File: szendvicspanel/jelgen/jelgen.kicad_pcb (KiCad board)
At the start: 2 copper layers, 23 parts, among them J1 Conn_01x04_Pin, U1 TL072, U2 TL072

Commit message: PCB sketch 2
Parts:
- removed TJ1, TJ2, TJ3: Conn_01x01_Pin, Connector_PinHeader_2.54mm:PinHeader_1x01_P2.54mm_Vertical
- added TP1: TestPoint, Connector_PinHeader_2.54mm:PinHeader_1x01_P2.54mm_Vertical, F.Cu at (149.0, 73.0)
- added TP2: TestPoint, Connector_PinHeader_2.54mm:PinHeader_1x01_P2.54mm_Vertical, F.Cu at (112.0, 66.0)
- added TP3: TestPoint, Connector_PinHeader_2.54mm:PinHeader_1x01_P2.54mm_Vertical, F.Cu at (112.0, 58.5)
- added TP4: TestPoint, Connector_PinHeader_2.54mm:PinHeader_1x01_P2.54mm_Vertical, F.Cu at (112.0, 73.5)
- J1: footprint Connector_PinHeader_2.54mm:PinHeader_1x04_P2.54mm_Horizontal -> Connector_PinHeader_2.54mm:PinHeader_1x04_P2.54mm_Vertical
- moved RV2 67.2 mm to (136.1, 65.3)
- moved U1 67.2 mm to (122.6, 62.4)
- moved C1 67.2 mm to (141.6, 52.4)
- moved R1 67.2 mm to (134.1, 58.4)
- moved R2 67.2 mm to (136.6, 74.9)
- moved R3 67.2 mm to (144.6, 60.9)
- moved RV3 67.2 mm to (142.6, 70.4)
- moved J1 45.3 mm to (78.0, 65.0), turned to 0 degrees
- moved C2 43.0 mm to (94.0, 75.0)
- moved R4 43.0 mm to (97.0, 67.0)
- moved RV1 43.0 mm to (90.9, 61.5)
- moved U2 42.0 mm to (101.0, 62.0)
- moved OJ1 13.9 mm to (78.0, 49.5)
- moved OJ2 13.9 mm to (85.5, 49.5)
- moved OJ3 13.9 mm to (93.0, 49.5)
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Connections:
- OJ1 pad 1: /PWM -> GND
- OJ1 pad 3: GND -> /OUT_ARRAY_PIN3
- OJ2 pad 1: /PWM -> GND
- OJ2 pad 3: GND -> /OUT_ARRAY_PIN3
- OJ3 pad 1: /PWM -> GND
- OJ3 pad 3: GND -> /OUT_ARRAY_PIN3
- OJ4 pad 1: /PWM -> GND
- OJ4 pad 3: GND -> /OUT_ARRAY_PIN3
- OJ5 pad 1: /PWM -> GND
- OJ5 pad 3: GND -> /OUT_ARRAY_PIN3
- OJ6 pad 1: /PWM -> GND
- OJ6 pad 3: GND -> /OUT_ARRAY_PIN3
- OJ7 pad 1: /PWM -> GND
- OJ7 pad 3: GND -> /OUT_ARRAY_PIN3
- OJ8 pad 1: /PWM -> GND
- OJ8 pad 3: GND -> /OUT_ARRAY_PIN3
- U2 pad 7: /PWM -> /OUT_ARRAY_PIN3
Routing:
- net /PWM: track 81.4 -> 0.00 mm
- net VPWR: track 215.8 -> 142.2 mm
- net /OUT_ARRAY_PIN3: track 0.00 -> 65.4 mm
- net /REF: track 63.1 -> 50.8 mm
- net /ANALOG_IN: track 22.3 -> 18.0 mm
- net /SQUARE: track 5.22 -> 6.42 mm
- net /TRIANGLE: track 34.1 -> 35.1 mm
- net Net-(U2A-+): track 12.8 -> 11.8 mm
- net GND: track 177.7 -> 178.4 mm
- net Net-(U1B-+): track 36.7 -> 37.4 mm
- net Net-(U1A--): track 30.9 -> 30.4 mm
- net Net-(U2B-+): track 20.2 -> 19.7 mm
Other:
- board outline added: 85 x 40 mm

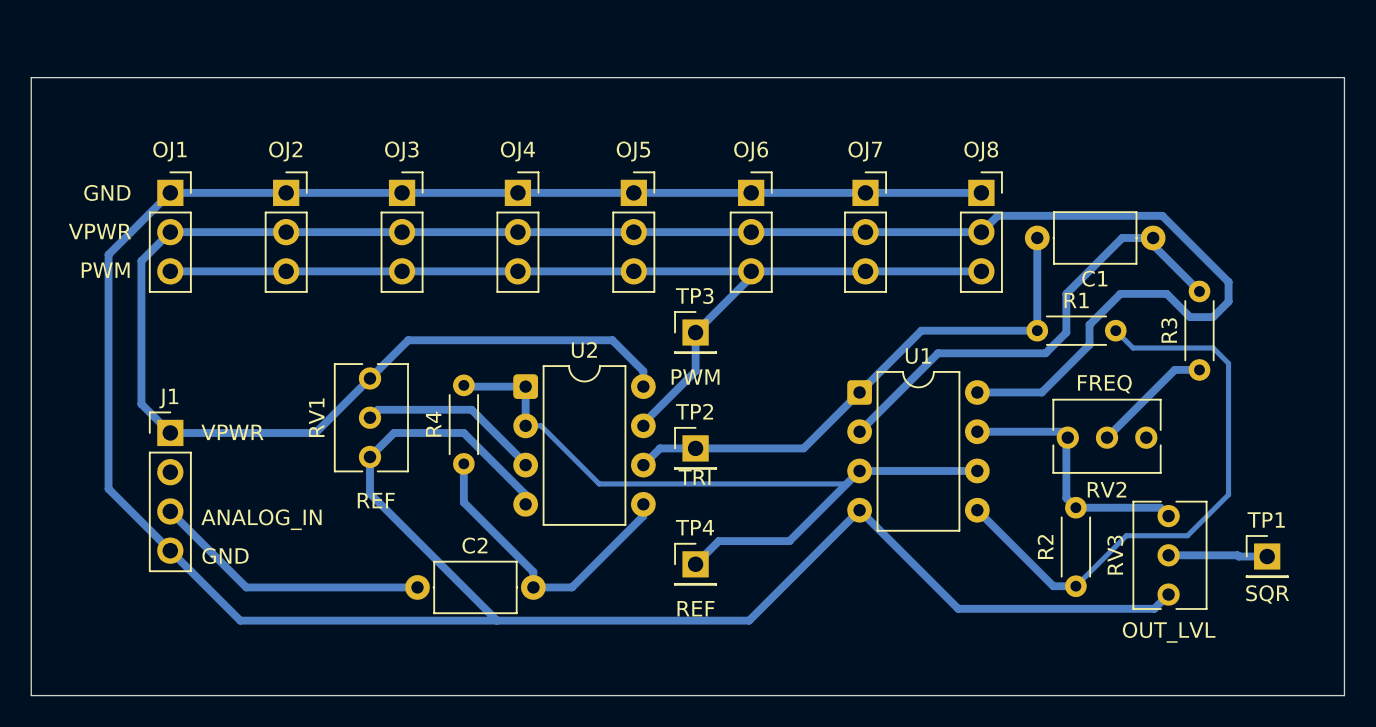
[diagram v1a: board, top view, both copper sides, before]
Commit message: Ground plane, output array áttervezés, input horizontal footprint
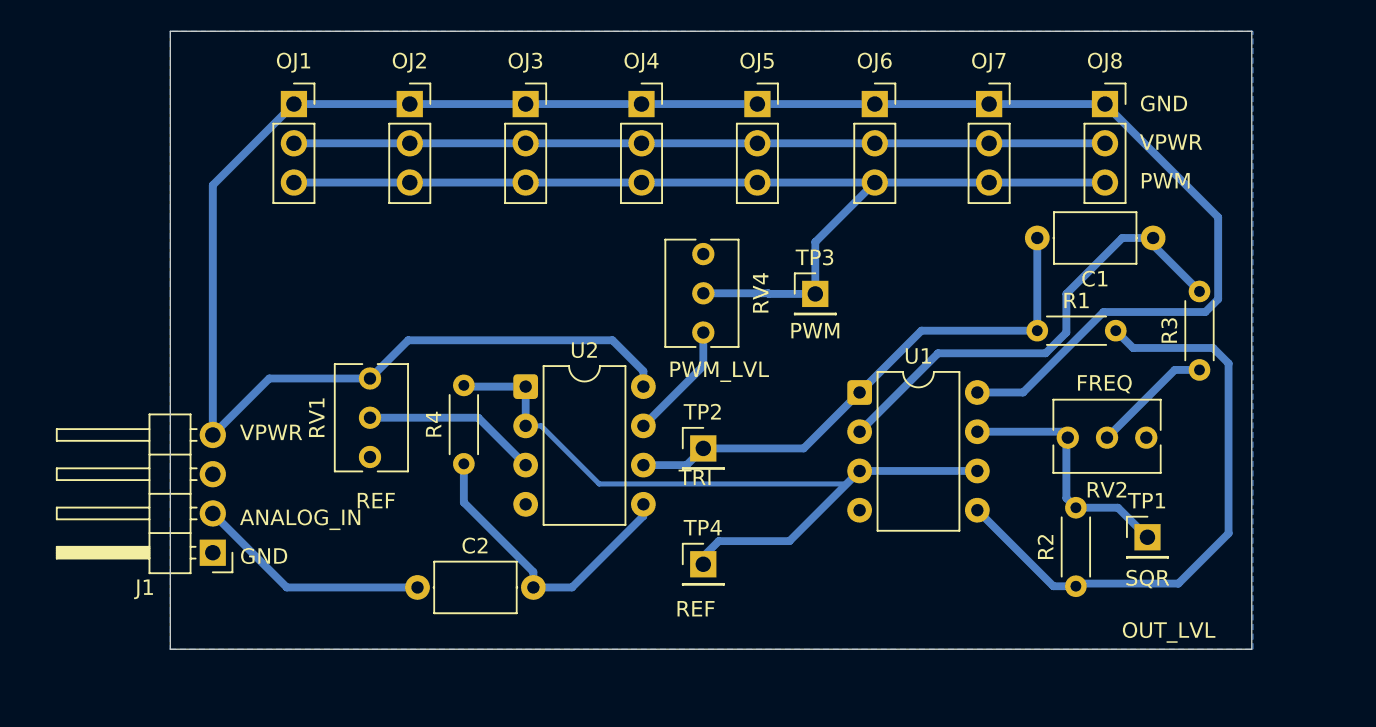
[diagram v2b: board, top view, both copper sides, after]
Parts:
- removed RV3: R_Potentiometer, Potentiometer_THT:Potentiometer_Bourns_3266Y_Vertical
- added RV4: R_Potentiometer, Potentiometer_THT:Potentiometer_Bourns_3266Y_Vertical, F.Cu at (112.5, 58.5)
- J1: footprint Connector_PinHeader_2.54mm:PinHeader_1x04_P2.54mm_Vertical -> Connector_PinHeader_2.54mm:PinHeader_1x04_P2.54mm_Horizontal
- moved OJ1 9.85 mm to (86.0, 43.7)
- moved OJ2 9.85 mm to (93.5, 43.7)
- moved OJ3 9.85 mm to (101.0, 43.7)
- moved OJ4 9.85 mm to (108.5, 43.7)
- moved OJ5 9.85 mm to (116.0, 43.7)
- moved OJ6 9.85 mm to (123.6, 43.7)
- moved OJ7 9.85 mm to (131.0, 43.7)
- moved OJ8 9.85 mm to (138.5, 43.7)
- moved J1 8.22 mm to (80.8, 72.8), turned to 180 degrees
- moved TP3 8.14 mm to (119.8, 56.0)
- moved TP1 7.85 mm to (141.2, 71.8)
- moved TP2 0.50 mm to (112.5, 66.0)
- moved TP4 0.50 mm to (112.5, 73.5)
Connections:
- J1 pad 1: VPWR -> GND
- J1 pad 2: unconnected-(J1-Pin_2-Pad2) -> /ANALOG_IN
- J1 pad 3: /ANALOG_IN -> unconnected-(J1-Pin_3-Pad3)
- J1 pad 4: GND -> VPWR
- OJ1 pad 1: GND -> VPWR
- OJ1 pad 2: VPWR -> GND
- OJ1 pad 3: /OUT_ARRAY_PIN3 -> /PWM
- OJ2 pad 1: GND -> VPWR
- OJ2 pad 2: VPWR -> GND
- OJ2 pad 3: /OUT_ARRAY_PIN3 -> /PWM
- OJ3 pad 1: GND -> VPWR
- OJ3 pad 2: VPWR -> GND
- OJ3 pad 3: /OUT_ARRAY_PIN3 -> /PWM
- OJ4 pad 1: GND -> VPWR
- OJ4 pad 2: VPWR -> GND
- OJ4 pad 3: /OUT_ARRAY_PIN3 -> /PWM
- OJ5 pad 1: GND -> VPWR
- OJ5 pad 2: VPWR -> GND
- OJ5 pad 3: /OUT_ARRAY_PIN3 -> /PWM
- OJ6 pad 1: GND -> VPWR
- OJ6 pad 2: VPWR -> GND
- OJ6 pad 3: /OUT_ARRAY_PIN3 -> /PWM
- OJ7 pad 1: GND -> VPWR
- OJ7 pad 2: VPWR -> GND
- OJ7 pad 3: /OUT_ARRAY_PIN3 -> /PWM
- OJ8 pad 1: GND -> VPWR
- OJ8 pad 2: VPWR -> GND
- OJ8 pad 3: /OUT_ARRAY_PIN3 -> /PWM
- R2 pad 2: Net-(R2-Pad2) -> /SQUARE
- RV2 pad 1: Net-(R2-Pad2) -> /SQUARE
- TP3 pad 1: /OUT_ARRAY_PIN3 -> /PWM
- U1 pad 7: Net-(R2-Pad2) -> /SQUARE
- U2 pad 7: /OUT_ARRAY_PIN3 -> Net-(RV4-Pad1)
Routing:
- net GND: track 178.4 -> 52.5 mm
- net /PWM: track 0.00 -> 68.9 mm
- net /OUT_ARRAY_PIN3: track 65.4 -> 0.00 mm
- net Net-(R2-Pad2): track 17.1 -> 0.00 mm
- net /SQUARE: track 6.42 -> 16.3 mm
- net Net-(RV4-Pad1): track 0.00 -> 7.65 mm
- net /ANALOG_IN: track 18.0 -> 15.2 mm
- net Net-(U1B-+): track 37.4 -> 38.9 mm
- added copper zone on B.Cu, net GND
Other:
- board size 85 x 40 mm -> 70 x 40 mm
- board text added: "PWM_LVL"

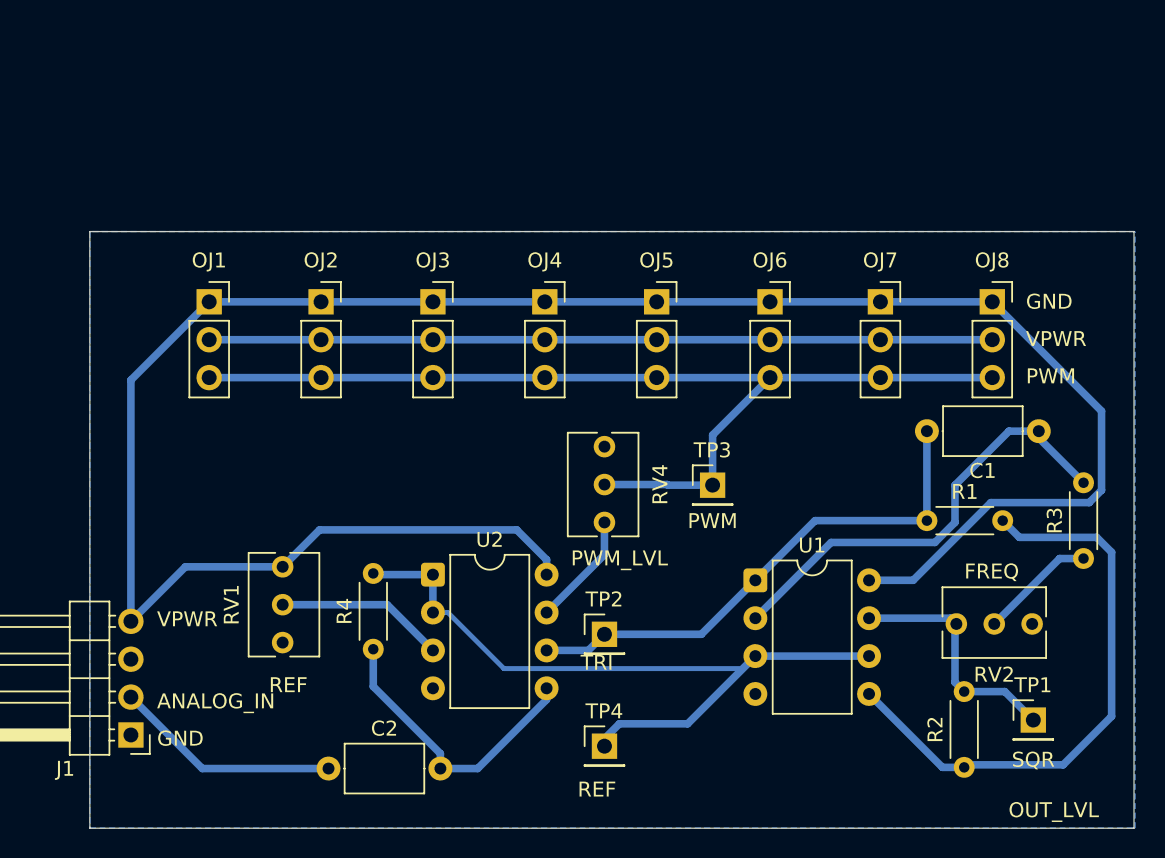
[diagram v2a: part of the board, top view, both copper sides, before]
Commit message: Átalakítás a H-híd panel szélességére, hanging +5V input pin
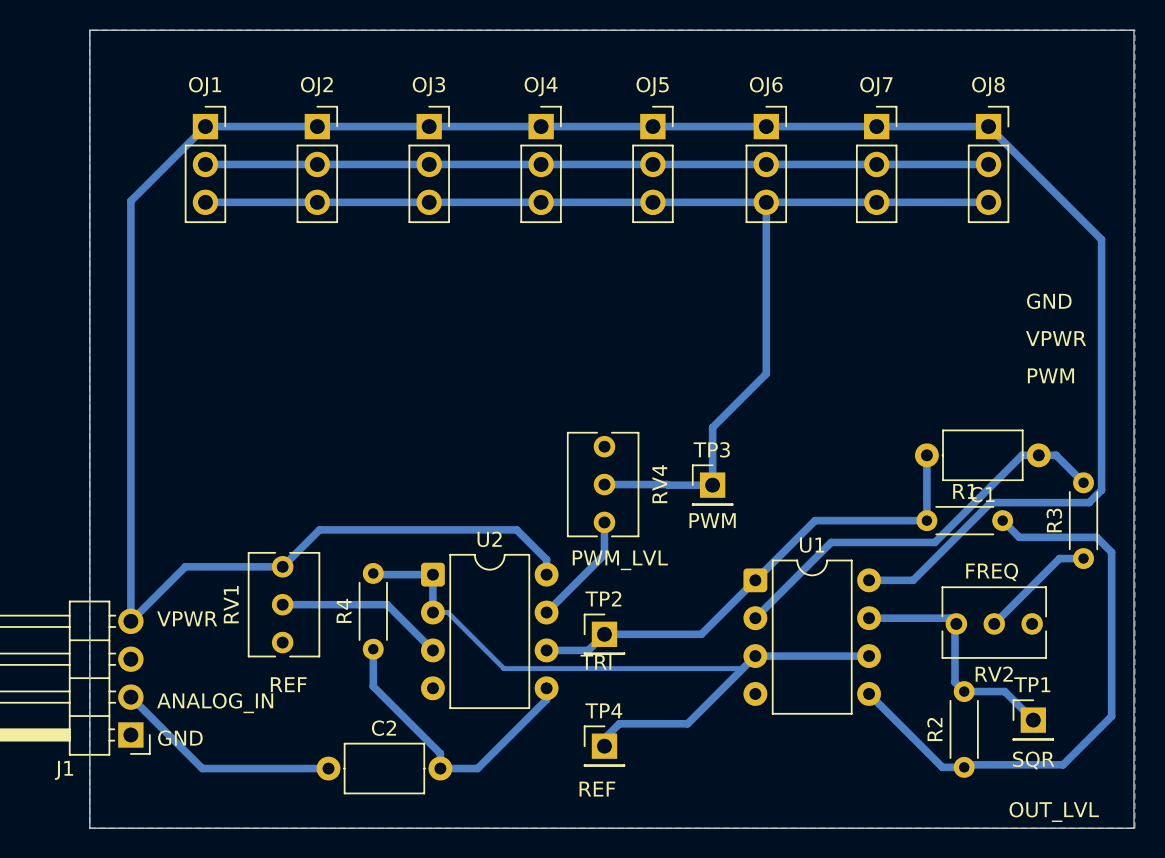
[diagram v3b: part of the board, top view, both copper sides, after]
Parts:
- moved OJ1 11.8 mm to (85.8, 32.0)
- moved OJ2 11.8 mm to (93.2, 32.0)
- moved OJ3 11.8 mm to (100.8, 32.0)
- moved OJ4 11.8 mm to (108.2, 32.0)
- moved OJ5 11.8 mm to (115.8, 32.0)
- moved OJ6 11.8 mm to (123.3, 32.0)
- moved OJ7 11.8 mm to (130.8, 32.0)
- moved OJ8 11.8 mm to (138.2, 32.0)
- moved C1 1.62 mm to (141.6, 54.0)
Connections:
- J1 pad 3: unconnected-(J1-Pin_3-Pad3) -> +5V
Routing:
- net VPWR: track 142.1 -> 165.6 mm
- net /PWM: track 68.9 -> 80.2 mm
- net Net-(U1A--): track 30.4 -> 27.3 mm
- net /TRIANGLE: track 35.1 -> 33.5 mm
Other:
- board size 70 x 40 mm -> 70 x 53.5 mm

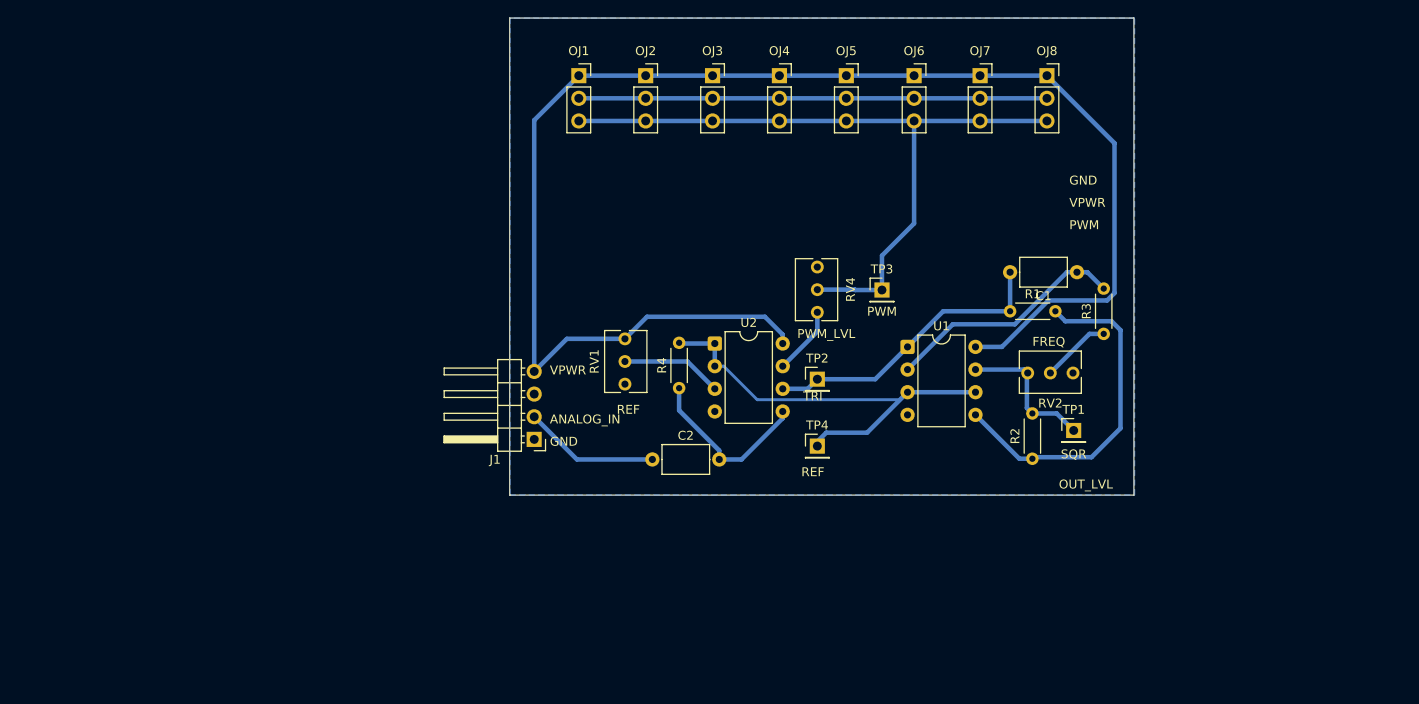
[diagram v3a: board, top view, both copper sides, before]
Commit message: [Kész] H-híd panel magasság, mérések, átrendezés
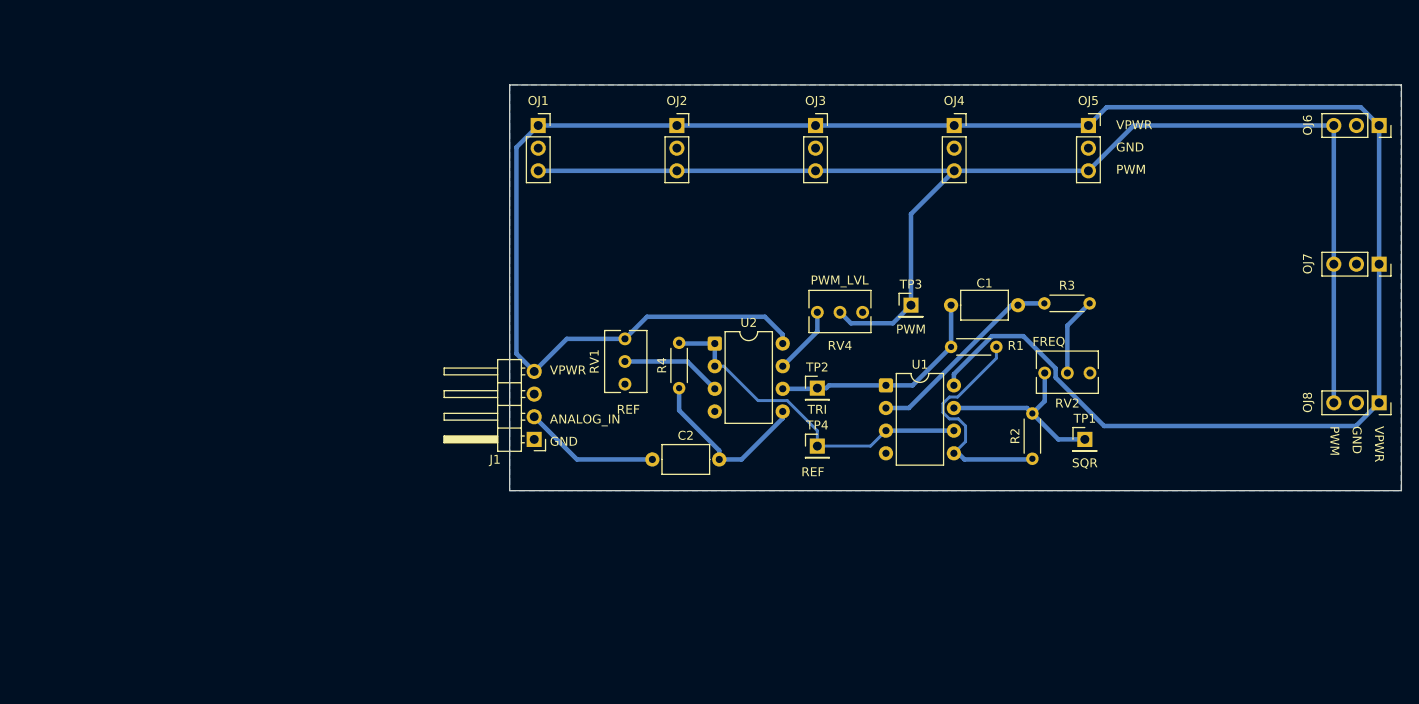
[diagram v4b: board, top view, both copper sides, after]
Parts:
- moved OJ7 63.4 mm to (175.5, 53.1), turned to -90 degrees
- moved OJ8 52.3 mm to (175.5, 68.7), turned to -90 degrees
- moved OJ6 45.1 mm to (175.5, 37.5), turned to -90 degrees
- moved OJ4 20.4 mm to (127.8, 37.5)
- moved OJ5 20.3 mm to (142.9, 37.5)
- moved OJ3 12.8 mm to (112.3, 37.5)
- moved R1 7.73 mm to (127.5, 62.4)
- moved C1 7.58 mm to (135.0, 57.7)
- moved OJ1 7.21 mm to (81.2, 37.5)
- moved OJ2 6.60 mm to (96.8, 37.5)
- moved U1 4.94 mm to (120.2, 66.7)
- moved R3 3.77 mm to (143.0, 57.5), turned to 180 degrees
- moved TP3 3.67 mm to (123.0, 57.7)
- moved RV2 1.91 mm to (138.0, 65.3)
- moved TP1 1.60 mm to (142.5, 72.8)
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- renumbered OJ6 to OJ5, OJ7 to OJ6, OJ5 to OJ7
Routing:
- net VPWR: track 165.6 -> 245.3 mm
- net /PWM: track 80.2 -> 148.8 mm
- net GND: track 52.5 -> 0.00 mm
- net Net-(U1B-+): track 38.9 -> 26.2 mm
- net /REF: track 50.6 -> 39.3 mm
- net /TRIANGLE: track 33.5 -> 25.5 mm
- net /SQUARE: track 16.3 -> 21.3 mm
- net Net-(U1A--): track 27.3 -> 22.6 mm
- net Net-(R3-Pad1): track 7.80 -> 8.84 mm
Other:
- board size 70 x 53.5 mm -> 100 x 45.5 mm
- board text removed: "OUT_LVL"
